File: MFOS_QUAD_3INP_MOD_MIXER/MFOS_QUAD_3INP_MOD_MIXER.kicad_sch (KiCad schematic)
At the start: 126 parts, among them J1 Barrel_Jack, J10 Barrel_Jack, J11 Barrel_Jack, J12 Barrel_Jack, J13 Barrel_Jack, J14 Barrel_Jack, J15 Barrel_Jack, J16 Barrel_Jack, J17 Barrel_Jack, J18 Barrel_Jack, J19 Barrel_Jack, J2 Barrel_Jack, J20 Barrel_Jack, J21 Conn_01x01, J22 Conn_01x01, J23 Conn_01x01, J24 Conn_01x01, J25 Conn_01x01, J26 Conn_01x01, J27 Conn_01x01, J28 Conn_01x01, J29 Conn_01x01, J3 Barrel_Jack, J30 Conn_01x01, J31 Conn_01x01, J32 Conn_01x01, J33 Conn_01x01, J34 Conn_01x01, J35 Conn_01x01, J36 Conn_01x01, J37 Conn_01x01, J38 Conn_01x01, J39 Conn_01x01, J4 Barrel_Jack, J40 Conn_01x01, J41 Conn_01x01, J42 Conn_01x01, J43 Conn_01x01, J44 Conn_01x01, J45 Conn_01x01, J46 Conn_01x01, J47 Conn_01x01, J5 Barrel_Jack, J6 Barrel_Jack, J7 Barrel_Jack, J8 Barrel_Jack, J9 Barrel_Jack, U1 TL074, U2 TL074, U3 TL074

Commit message: Reviewed BOM
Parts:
- J1, J10, J11, J12, J13, J14, J15, J16, J17, J18, J19, J2, J20, J3, J4, J5, J6, J7, J8, J9: symbol Connector:Barrel_Jack -> Connector:Jack-DC
- J21, J22, J23, J24, J25, J26, J27, J28, J29, J30, J31, J32, J33, J34, J35, J36, J37, J38, J39, J40, J41, J42, J43, J44, J45, J46, J47: now left out of the parts list

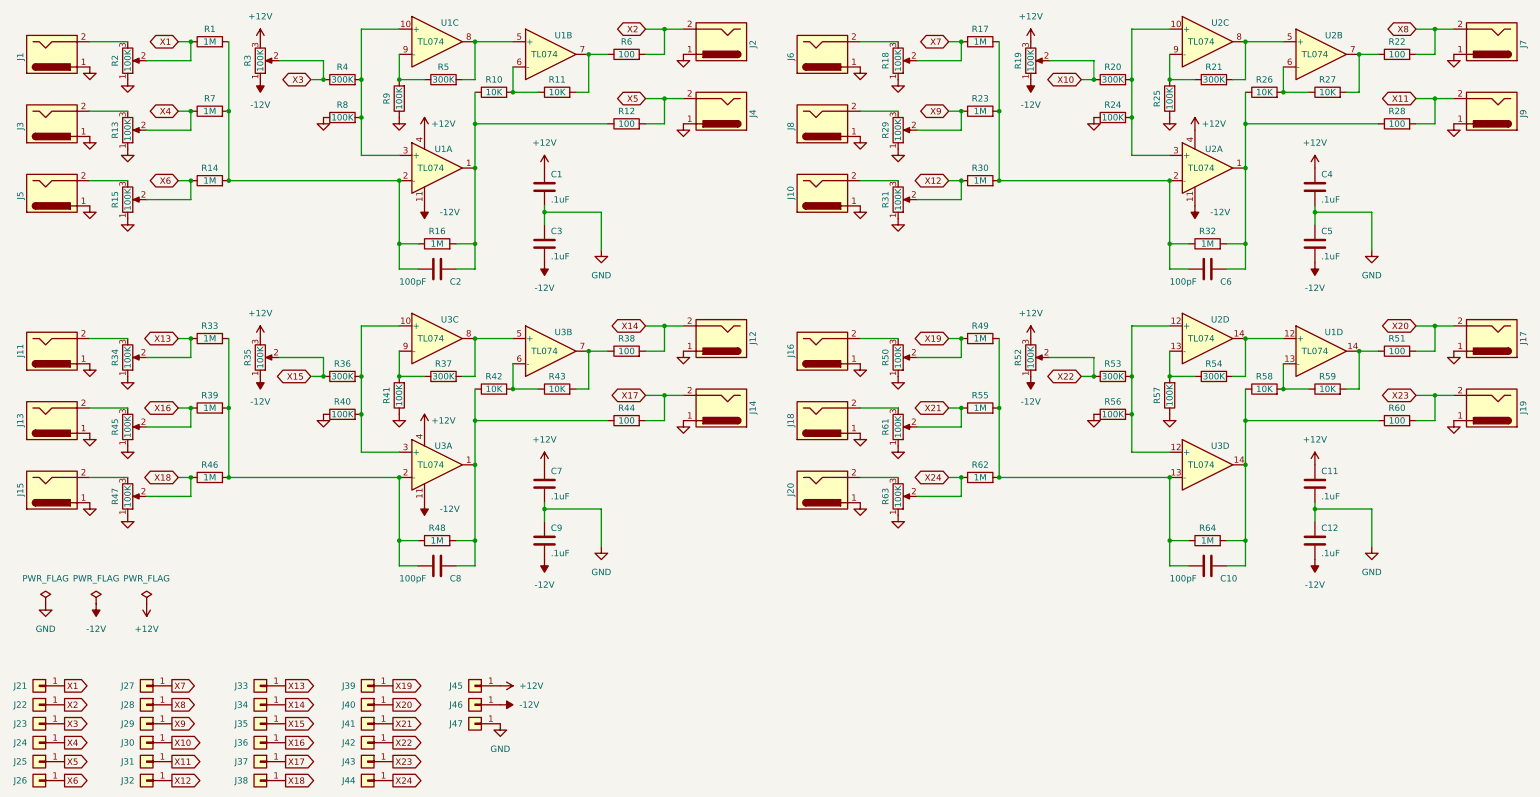
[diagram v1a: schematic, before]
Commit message: Designs adapted for BOM
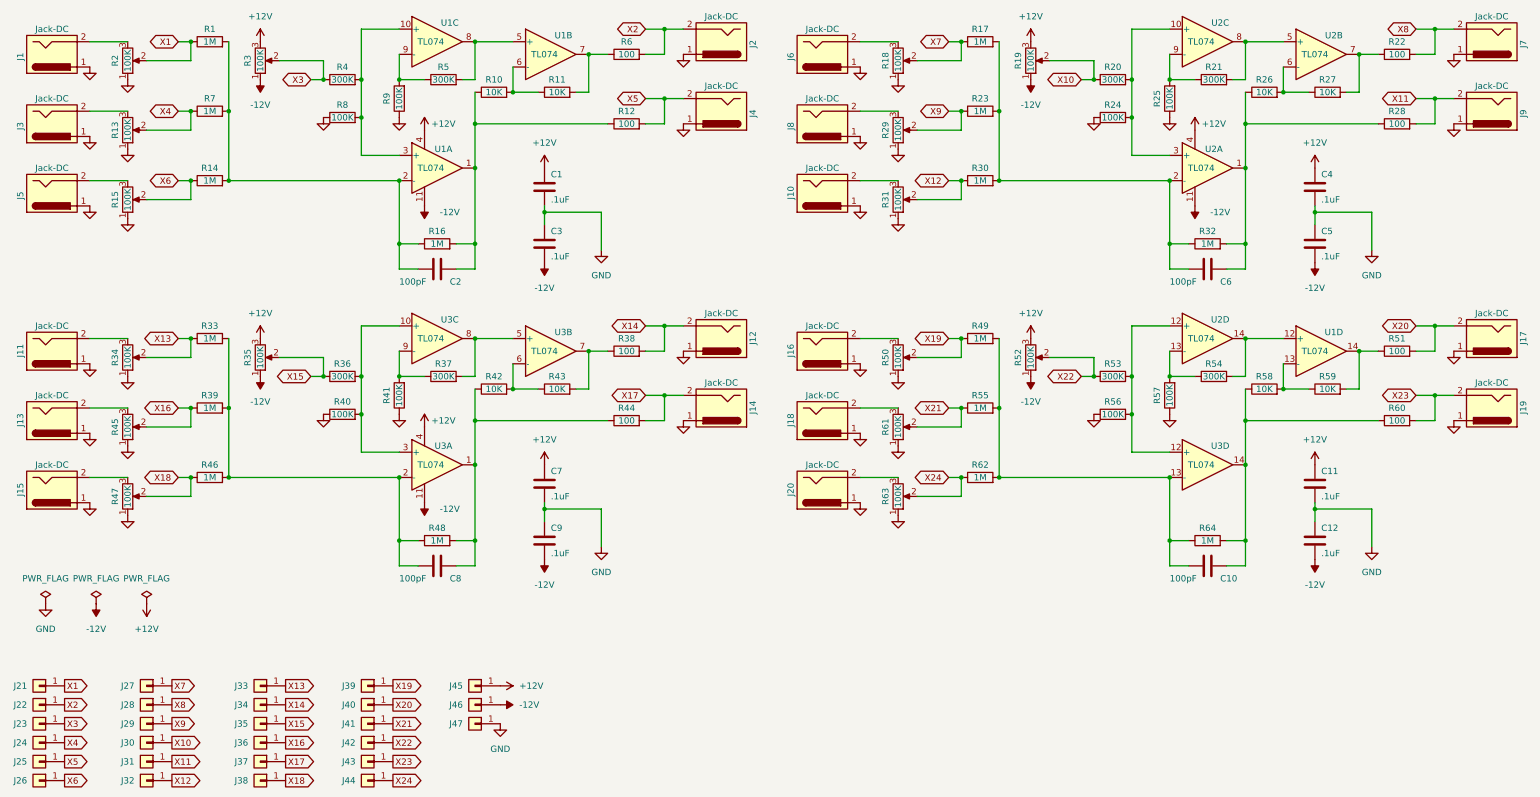
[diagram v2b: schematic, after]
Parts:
- J1, J10, J11, J12, J13, J14, J15, J16, J17, J18, J19, J2, J20, J3, J4, J5, J6, J7, J8, J9: value Barrel_Jack -> Jack-DC
